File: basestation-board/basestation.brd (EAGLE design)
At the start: 73.4 x 45.5 mm, 69 parts, among them IC1 STM32F0, IC2 MCP1700TT, IC3 MCP73831, IC4 MCP1700TT, J1 SWD_PTH_SHROUD, Q1 BSS84, Q2 BSS84, SW1 ROTARTY_ENCODER, U1 NHD-C0216CIZ-FSW, U2 RFM98, U3 RN4020, X1 BU-SMA-V, X2 CRYSTAL-GROUNDED

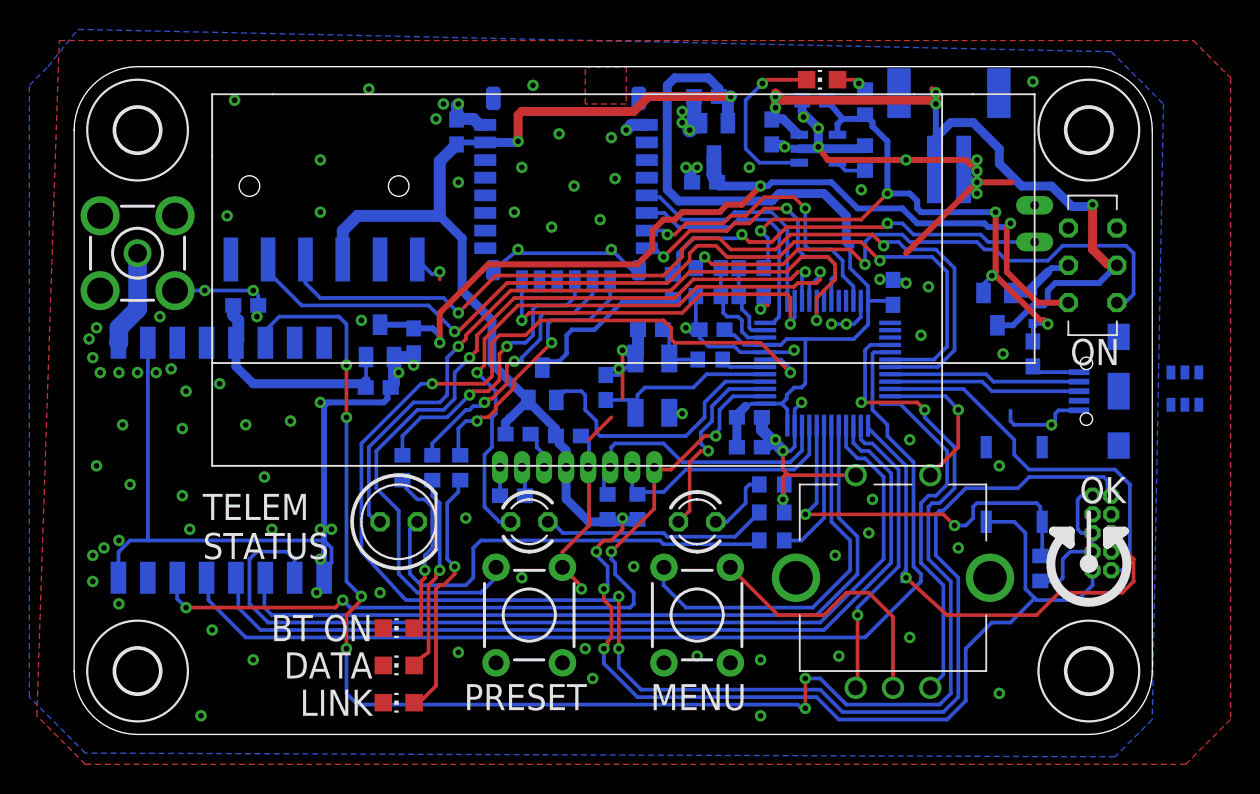
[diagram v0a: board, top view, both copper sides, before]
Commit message: added esd protection
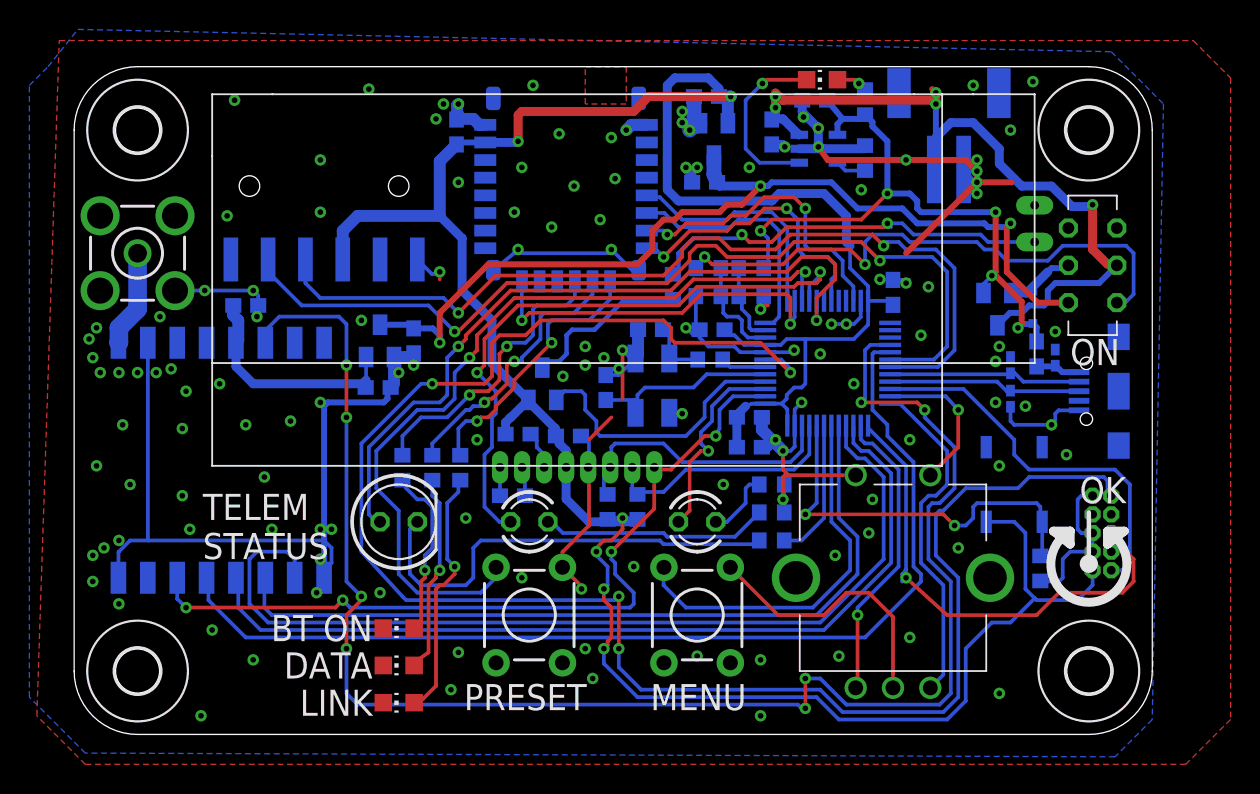
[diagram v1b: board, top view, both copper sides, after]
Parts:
- removed U$3: NUP2114UCMR6T1G, Mine:TSOP6
- added D2, D3, D4: RB751, SparkFun-DiscreteSemi:SOD-523
- moved L1 0.25 mm to (65.0, 25.4)
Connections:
- net DM: now also D2.C; no longer U$3.1
- net DP: now also D3.C; no longer U$3.6
- net GND: now also D2.A, D3.A, D4.A; no longer U$3.2
- net N$35: now also D4.C; no longer U$3.5
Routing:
- net GND: vias 117 -> 133

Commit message: finishing off
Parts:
- removed R11, R12, R14, R15, R2, R3, R6, R7, R8, R9: (no value), resistor:R0603
- added RN1, RN2: 330, resistor-dil:EXB38V
- added RN3: 10k, resistor-dil:EXB38V
- J1: value SWD_PTH_SHROUD -> SWD_SHROUD_SMD; device dtb:SWD_PTH_SHROUD -> dtb:SWD_SMD_SHROUD
- R13: value (none) -> 22
- R4, R5: value (none) -> 4k7
- moved S3 1.02 mm to (62.5, 16.5)
- moved R1 0.80 mm to (64.5, 11.0)
- moved R17 0.25 mm to (53.6, 42.5)
- moved R10 0.13 mm to (42.9, 25.0)
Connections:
- net AIN1: now also RN3.5, RN3.6; no longer R11.2, R14.1
- net GND: now also RN2.1, RN2.2, RN2.3, RN3.2, RN3.3; no longer R11.1, R12.1, R3.1, R6.1
- net LED4: now also RN2.4; no longer R2.1
- net N$10: now also RN2.7; no longer R6.2
- net N$11: now also RN2.5; no longer R2.2
- net N$13: now also RN1.7; no longer R8.2
- net N$14: now also RN1.6; no longer R9.2
- net N$15: now also RN1.1; no longer R7.1
- net N$16: now also RN1.2; no longer R8.1
- net N$17: now also RN1.3; no longer R9.1
- net N$27: now also RN3.7, RN3.8; no longer R12.2, R15.1
- net N$5: now also RN1.8; no longer R7.2
- net N$6: now also RN2.6; no longer R3.2
- net VBAT_S: now also RN3.1; no longer R15.2
- net VBUS: now also RN3.4; no longer R14.2
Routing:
- net GND: track 213.9 -> 205.0 mm, vias 133 -> 144
- net SWDAT: track 26.4 -> 29.6 mm, vias 0 -> 2
- net N$14: track 20.1 -> 18.4 mm
- net SW2: track 55.2 -> 53.7 mm
- net SWCLK: track 32.9 -> 31.4 mm, vias 1 -> 2
- net N$27: track 7.12 -> 5.71 mm
- net N$10: track 4.61 -> 3.23 mm
- net +3V3: track 192.7 -> 191.3 mm
- net 3.3V: track 15.9 -> 17.2 mm
- net N$17: track 11.9 -> 10.6 mm
- net N$4: track 27.7 -> 26.6 mm
- net LED3: track 50.2 -> 49.1 mm
- net VBUS: track 44.7 -> 45.6 mm
- net AIN1: track 5.47 -> 4.58 mm
- net RST: track 121.3 -> 122.1 mm
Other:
- board text added: "SWD"
